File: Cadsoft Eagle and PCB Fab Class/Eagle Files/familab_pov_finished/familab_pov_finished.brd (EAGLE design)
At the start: 58.4 x 42.9 mm, 10 parts, among them U1 Tiny85-20-SMT

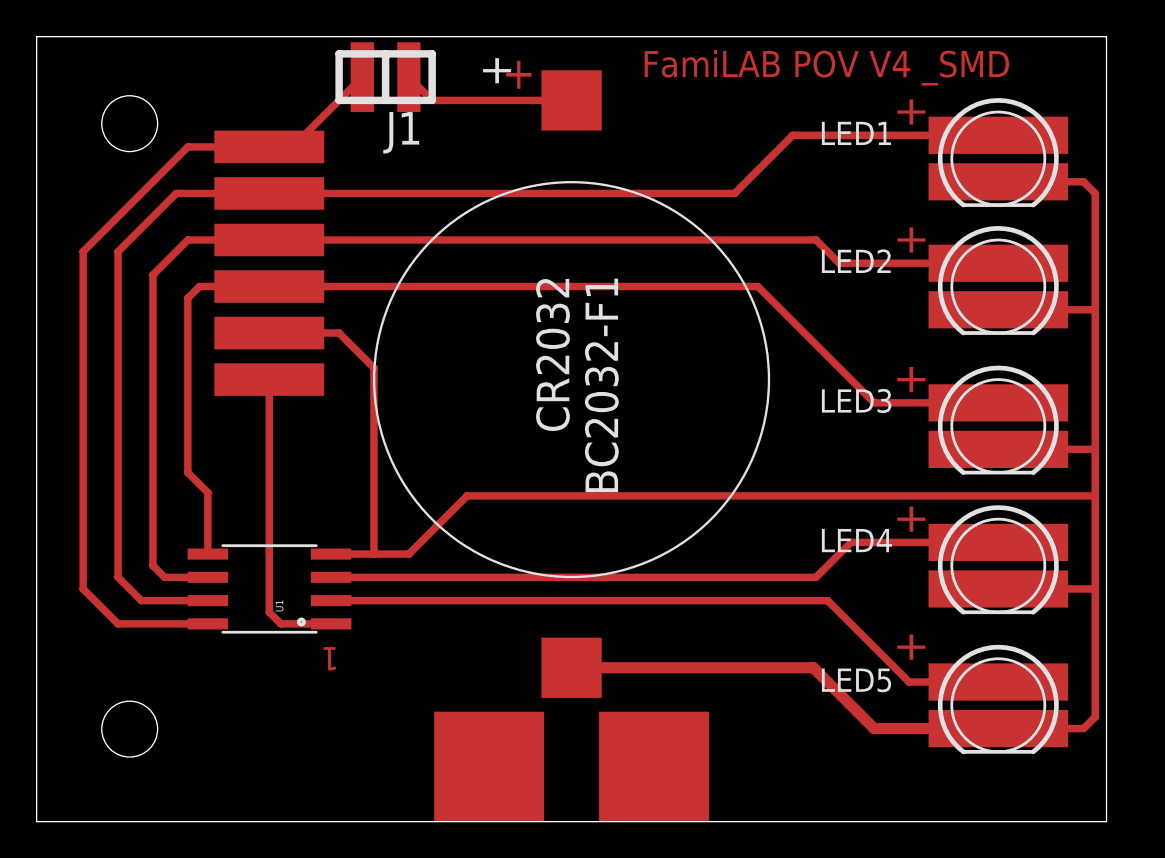
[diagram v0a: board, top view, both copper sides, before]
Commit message: Increased Dimensions slightly and Fixed Arduino Code
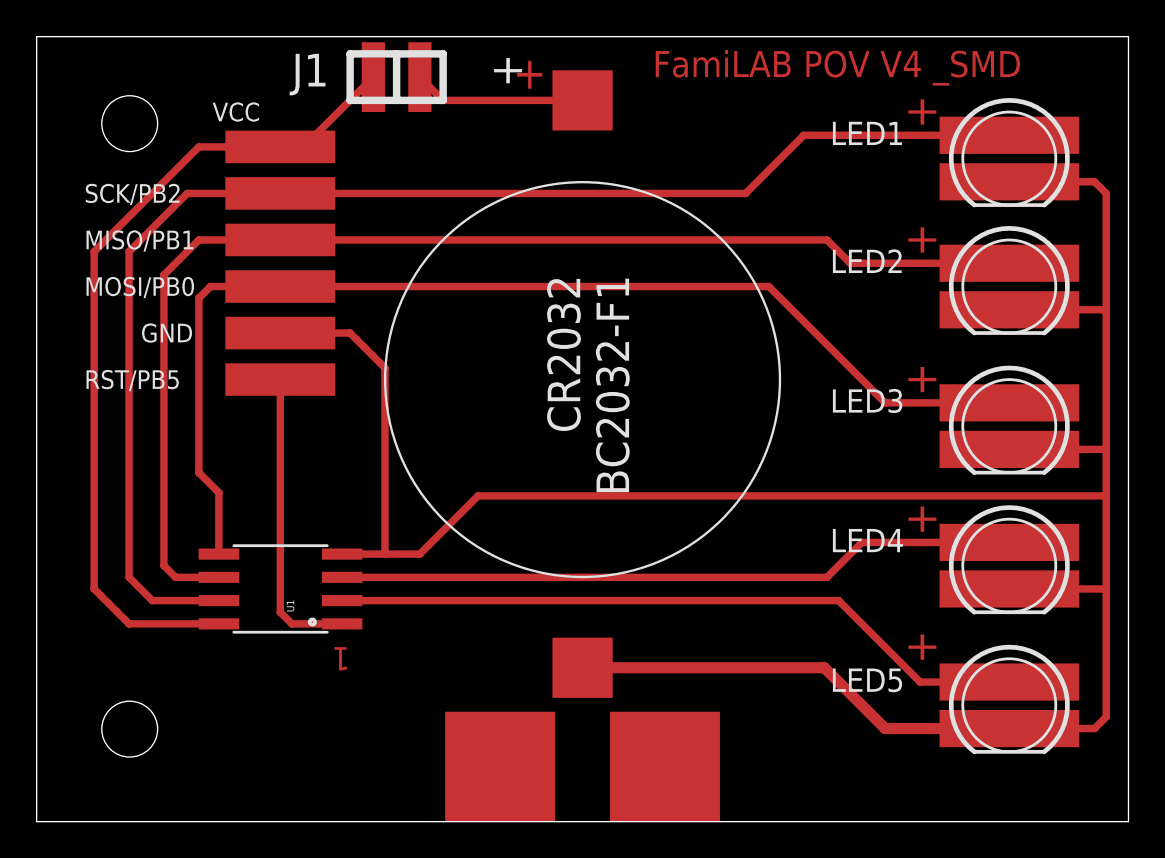
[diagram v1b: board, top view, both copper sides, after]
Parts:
- J1: device fri-001:JUMPER_SMD_SIDE -> pov_class:JUMPER_SMD_SIDE
- moved LED1 0.60 mm to (53.1, 36.2)
- moved LED2 0.60 mm to (53.1, 29.2)
- moved LED3 0.60 mm to (53.1, 21.6)
- moved LED4 0.60 mm to (53.1, 14.0)
- moved LED5 0.60 mm to (53.1, 6.35)
- moved U$1 0.60 mm to (29.8, 39.4)
- moved U$2 0.60 mm to (29.8, 3.00)
- moved U$4 0.60 mm to (13.3, 29.2)
- moved U1 0.60 mm to (13.3, 12.7)
- moved J1 0.60 mm to (18.4, 40.6)
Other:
- board size 58.4 x 42.9 mm -> 59.6 x 42.9 mm
- board text added: "GND"
- board text added: "MISO/PB1"
- board text added: "MOSI/PB0"
- board text added: "RST/PB5"
- board text added: "SCK/PB2"
- board text added: "VCC"

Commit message: Updates
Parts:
- J1: device pov_class:JUMPER_SMD_SIDE -> pov_class_finished:JUMPER_SMD_SIDE
- U$4: device pov_class:POV_ISP_CONNECTOR -> pov_class_finished:POV_ISP_CONNECTOR
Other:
- board text removed: "GND"
- board text removed: "MISO/PB1"
- board text removed: "MOSI/PB0"
- board text removed: "RST/PB5"
- board text removed: "SCK/PB2"
- board text removed: "VCC"
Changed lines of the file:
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@@
 <?xml version="1.0" encoding="utf-8"?>
 <!DOCTYPE eagle SYSTEM "eagle.dtd">
-<eagle version="6.4">
+<eagle version="6.5.0">
 <drawing>
 <settings>
@@
 <circle x="5.08" y="5.08" radius="0.635" width="0.4064" layer="1"/>
 <circle x="5.08" y="38.1" radius="0.635" width="0.4064" layer="1"/>
-<text x="9.6" y="38.735" size="1.016" layer="25" align="center-left">VCC</text>
-<text x="2.6" y="34.29" size="1.016" layer="25" font="vector" align="center-left">SCK/PB2</text>
-<text x="2.6" y="31.75" size="1.016" layer="25" font="vector" align="center-left">MISO/PB1</text>
-<text x="2.6" y="29.21" size="1.016" layer="25" font="vector" align="center-left">MOSI/PB0</text>
-<text x="5.68" y="26.67" size="1.016" layer="25" font="vector" align="center-left">GND</text>
-<text x="2.6" y="24.13" size="1.016" layer="25" font="vector" align="center-left">RST/PB5</text>
 </plain>
 <attributes>
@@
 <attribute name="PROD_ID" value="IC-09092" x="13.3" y="12.7" size="1.778" layer="27" rot="R90" display="off"/>
 </element>
-<element name="J1" library="pov_class" package="JUMPER_SMD_SIDE" value="" x="18.38" y="40.64" smashed="yes" rot="R180">
+<element name="J1" library="pov_class_finished" package="JUMPER_SMD_SIDE" value="" x="18.38" y="40.64" smashed="yes" rot="R180">
 <attribute name="NAME" x="15.967" y="41.91" size="1.778" layer="21" rot="R180"/>
 </element>
 <element name="U$2" library="pov_class" package="MOUNTING_PADS" value="MOUNTING_PAD" x="29.8" y="3"/>
-<element name="U$4" library="pov_class" package="POV_ISP_CONNECTOR" value="ICSP_PROGRAM" x="13.3" y="29.21"/>
+<element name="U$4" library="pov_class_finished" package="POV_ISP_CONNECTOR" value="ICSP_PROGRAM" x="13.3" y="29.21"/>
 </elements>
 <signals>
